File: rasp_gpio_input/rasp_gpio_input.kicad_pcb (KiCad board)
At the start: 2 copper layers, 23.5 x 46.6 mm, 22 parts, among them J1 Conn_01x06, J2 Conn_01x04, J3 Conn_01x15, J4 Conn_01x15_Male, J5 Conn_01x15_Male

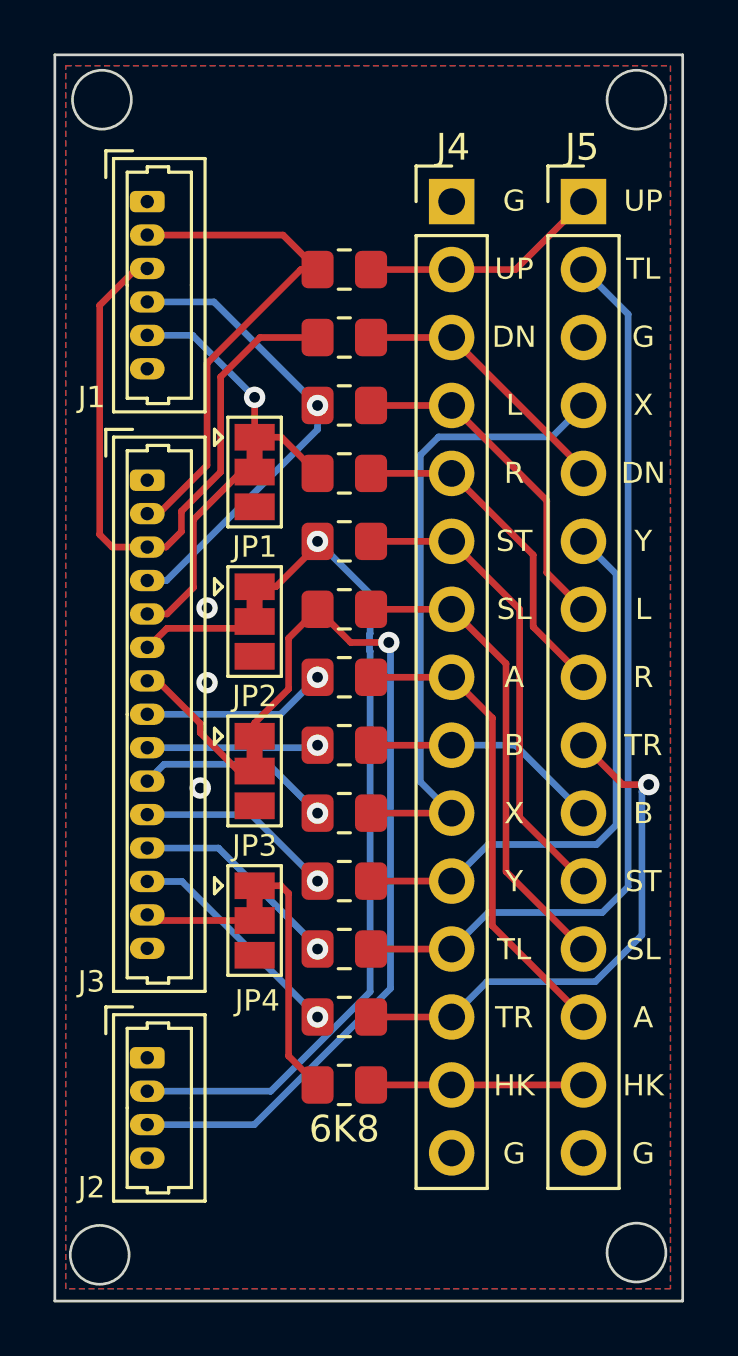
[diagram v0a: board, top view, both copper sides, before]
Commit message: rasp_gpio 배선 최적화
Signed-off-by: Ju, Gyeong-min <jcmh74@gmail.com>
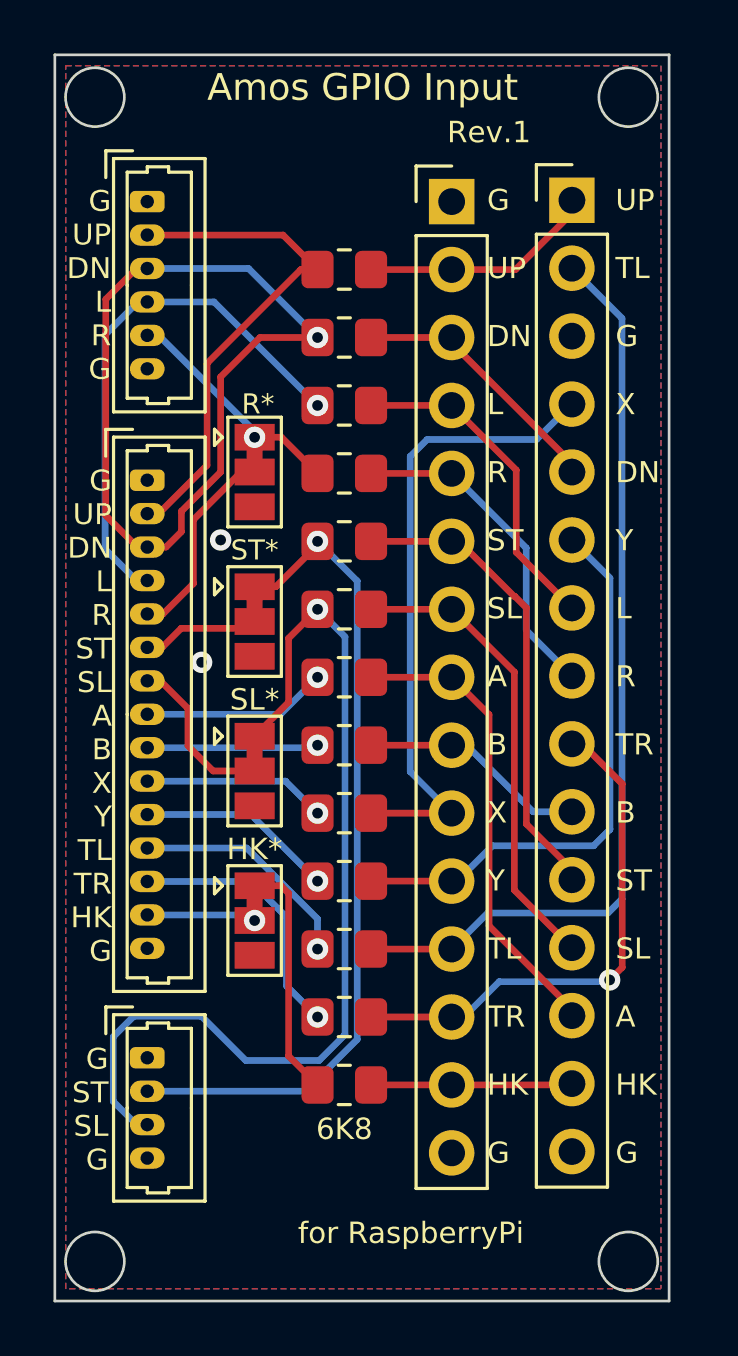
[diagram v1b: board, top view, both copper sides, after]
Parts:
- moved J5 0.43 mm to (149.0, 85.6)
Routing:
- net /DOWN: track 25.0 -> 31.7 mm, vias 0 -> 1
- net /SELECT: track 33.1 -> 36.2 mm
- net /LEFT: track 17.6 -> 20.1 mm
- net /TR: track 8.46 -> 9.97 mm
- net /RIGHT: track 9.38 -> 8.63 mm
- net /C_TR: track 20.2 -> 19.5 mm
- net /TL: track 7.97 -> 8.59 mm
- net /SELECT_T: track 5.61 -> 6.23 mm
- net /X: track 7.39 -> 6.86 mm
- net /HK_T: vias 0 -> 1
- net /GND: vias 3 -> 2
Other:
- board size 23.5 x 46.6 mm -> 23 x 46.6 mm
- board text added: "Amos GPIO Input"
- board text added: "G ST SL G"
- board text added: "G UP DN L R G"
- board text added: "HK*"
- board text added: "R*"
- board text added: "Rev.1"
- board text added: "SL*"
- board text added: "ST*"
- board text added: "for RaspberryPi"
